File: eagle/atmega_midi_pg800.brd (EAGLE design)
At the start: 101 x 81 mm, 19 parts, among them IC1 78L05Z, U1 6N138, U2 ATMEGA328P_PDIP, X1 MAB6H

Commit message: routed
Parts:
- removed MIDI_IN1: MIDIJACK, adafruit:CP-2350
- removed RESET2: LSP11, solpad:LSP11
- added C4: 100uF, rcl:B45181A
- added C5: 10uF, rcl:B45181A
- added MIDI_THRU: MIDIJACK, adafruit:CP-2350
- added X2: 22-23-2081, con-molex:22-23-2081
- RESET: value LSP11 -> 22-23-2021; device solpad:LSP11 -> con-molex:22-23-2021
- moved D2 106.2 mm to (54.6, 17.8)
- moved IC1 102.8 mm to (45.7, 22.9), turned to 270 degrees
- moved X1 85.7 mm to (63.5, 7.62)
- moved R5 50.8 mm to (31.8, 19.1)
- moved RESET 6.14 mm to (24.1, 23.6), turned to 90 degrees
- moved R24 5.58 mm to (61.0, 21.6)
- moved D1 2.84 mm to (4.45, 26.0)
- moved R3 2.54 mm to (19.1, 30.5)
- moved C2 2.03 mm to (69.1, 24.1), turned to 90 degrees
- moved C3 1.98 mm to (30.5, 34.5), turned to 0 degrees
- moved R1 1.80 mm to (22.9, 31.8)
- moved U1 1.80 mm to (12.1, 27.3)
- moved Q1 1.80 mm to (61.0, 25.4)
- moved C1 0.25 mm to (53.1, 24.1), turned to 90 degrees
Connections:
- removed net PE: X1.PE, X1.PE@
- new net N$10: U2.16, X1.1
- new net N$11: U2.15, X1.5
- new net N$12: U2.23, X2.7
- new net N$13: U2.24, X2.6
- new net N$14: U2.25, X2.5
- new net N$15: U2.26, X2.4
- new net N$16: U2.27, X2.3
- new net N$17: U2.28, X2.2
- new net N$2: D2.A, X1.3
- new net N$6: C4.+, D2.C, IC1.3
- new net N$9: U2.14, X1.6
- net +5V: now also C5.+, IC1.1, X2.1
- net GND: now also C4.-, C5.-, IC1.2, MIDI_THRU.2, MIDI_THRU.PE, MIDI_THRU.PE1, MIDI_THRU.PE2, MIDI_THRU.PE@, RESET.1, X1.4, X1.PE, X1.PE@, X2.8; no longer MIDI_IN1.2, MIDI_IN1.PE, MIDI_IN1.PE1, MIDI_IN1.PE2, MIDI_IN1.PE@, RESET2.MP
- net N$1: now also MIDI_THRU.4; no longer MIDI_IN1.4
- net N$42: now also MIDI_THRU.5; no longer MIDI_IN1.5
- net N$43: now also RESET.2; no longer RESET.MP
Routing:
- net N$11: track 0.00 -> 49.1 mm
- net +5V: track 55.3 -> 86.3 mm
- net N$10: track 0.00 -> 27.2 mm
- net N$9: track 0.00 -> 20.1 mm
- net N$42: track 0.00 -> 19.9 mm
- net GND: track 226.8 -> 215.6 mm, vias 4 -> 0
- net N$6: track 0.00 -> 9.40 mm
- net N$7: track 23.9 -> 14.9 mm
- net N$2: track 0.00 -> 6.35 mm
- net N$3: track 21.7 -> 16.2 mm
- net N$43: track 11.4 -> 16.6 mm
- net N$17: track 0.00 -> 5.08 mm
- net N$16: track 0.00 -> 5.08 mm
- net N$15: track 0.00 -> 5.08 mm
- net N$14: track 0.00 -> 5.08 mm
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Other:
- board size 101 x 81 mm -> 100 x 80.8 mm

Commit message: gcode
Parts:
- Q1: value (none) -> 16.000Mhz
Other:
- outline, holes or cut-outs redrawn

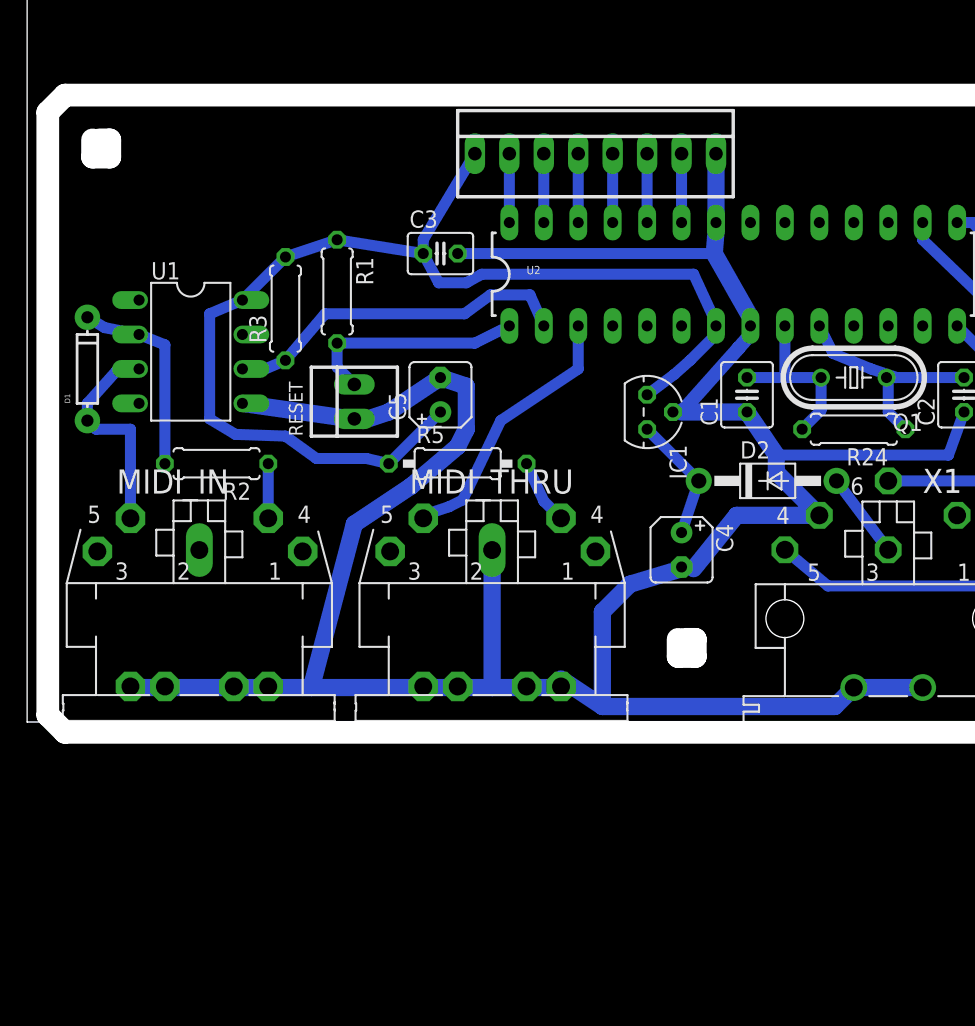
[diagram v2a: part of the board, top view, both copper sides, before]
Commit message: added oled disply connection
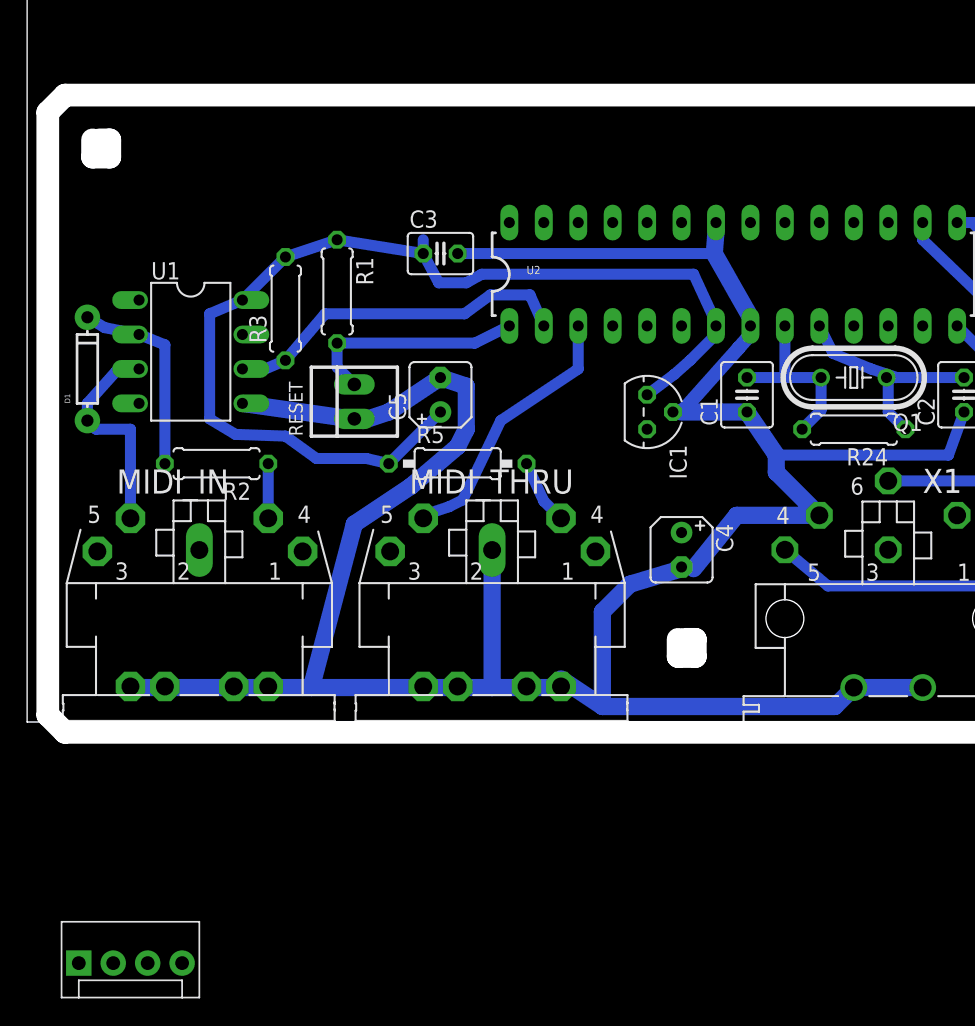
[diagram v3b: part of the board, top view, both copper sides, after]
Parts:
- removed D2: 1N4004, adafruit:DO41-10
- removed X2: 22-23-2081, con-molex:22-23-2081
- added DISPLAY: (no value), SparkFun-Connectors:MOLEX-1X4
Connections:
- removed net N$14: U2.25, X2.5
- removed net N$15: U2.26, X2.4
- removed net N$16: U2.27, X2.3
- removed net N$17: U2.28, X2.2
- removed net N$2: D2.A, X1.3
- net +5V: now also DISPLAY.1; no longer X2.1
- net GND: now also DISPLAY.2; no longer X2.8
- net N$12: now also DISPLAY.3, U2.28; no longer U2.23, X2.7
- net N$13: now also DISPLAY.4, U2.27; no longer U2.24, X2.6
- net N$6: now also X1.3; no longer D2.C
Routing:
- net N$6: track 9.40 -> 0.00 mm
- net +5V: track 86.3 -> 78.9 mm
- net N$2: track 6.35 -> 0.00 mm
- net N$17: track 5.08 -> 0.00 mm
- net N$16: track 5.08 -> 0.00 mm
- net N$15: track 5.08 -> 0.00 mm
- net N$14: track 5.08 -> 0.00 mm
- net N$13: track 5.08 -> 0.00 mm
- net N$12: track 5.08 -> 0.00 mm
- net GND: track 215.6 -> 210.5 mm
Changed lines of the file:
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@@
 <?xml version="1.0" encoding="utf-8"?>
 <!DOCTYPE eagle SYSTEM "eagle.dtd">
-<eagle version="7.6.0">
+<eagle version="7.7.0">
 <drawing>
 <settings>
@@
 </element>
 <element name="IC1" library="linear" package="TO92" value="78L05Z" x="45.72" y="22.86" rot="R270"/>
-<element name="D2" library="adafruit" package="DO41-10" value="1N4004" x="54.61" y="17.78"/>
 <element name="C4" library="rcl" package="B45181A" value="100uF" x="48.26" y="12.7" rot="R270"/>
 <element name="C5" library="rcl" package="B45181A" value="10uF" x="30.48" y="24.13" rot="R90"/>
@@
 <attribute name="MF" value="MOLEX" x="16.51" y="16.002" size="1.778" layer="27" rot="R90" display="off"/>
 </element>
-<element name="X2" library="con-molex" package="22-23-2081" value="22-23-2081" x="41.91" y="41.91">
-<attribute name="OC_NEWARK" value="01C7592" x="41.91" y="41.91" size="1.778" layer="27" display="off"/>
-<attribute name="MPN" value="22-23-2081" x="41.91" y="41.91" size="1.778" layer="27" display="off"/>
-<attribute name="OC_FARNELL" value="1756826" x="41.91" y="41.91" size="1.778" layer="27" display="off"/>
-<attribute name="MF" value="MOLEX" x="41.91" y="41.91" size="1.778" layer="27" display="off"/>
-</element>
+<element name="DISPLAY" library="SparkFun-Connectors" package="MOLEX-1X4" value="" x="3.81" y="-17.78"/>
 </elements>
 <signals>
@@
 <wire x1="30.353" y1="32.385" x2="32.385" y2="32.385" width="0.8128" layer="16"/>
 <wire x1="29.21" y1="34.544" x2="30.353" y2="32.385" width="0.8128" layer="16"/>
-<wire x1="33.02" y1="41.91" x2="29.21" y2="35.56" width="0.8128" layer="16"/>
 <wire x1="29.21" y1="35.56" x2="29.21" y2="34.544" width="0.8128" layer="16"/>
-<contactref element="X2" pad="1"/>
+<contactref element="DISPLAY" pad="1"/>
+<wire x1="3.81" y1="-17.78" x2="15.367" y2="21.209" width="0" layer="19" extent="16-16"/>
 </signal>
 <signal name="N$30">
@@
 <wire x1="55.245" y1="18.415" x2="58.42" y2="15.24" width="1.27" layer="16"/>
 <wire x1="17.78" y1="2.62" x2="15.24" y2="2.62" width="0.8128" layer="16"/>
-<contactref element="X2" pad="8"/>
-<wire x1="50.8" y1="41.91" x2="50.8" y2="36.83" width="1.27" layer="16"/>
+<contactref element="DISPLAY" pad="2"/>
+<wire x1="7.62" y1="2.54" x2="6.35" y2="-17.78" width="0" layer="19" extent="16-16"/>
 </signal>
 <signal name="N$42">
@@
 <wire x1="38.1" y1="16.29" x2="39.37" y2="15.02" width="0.8128" layer="16"/>
 </signal>
-<signal name="N$2">
-<contactref element="X1" pad="3"/>
-<contactref element="D2" pad="A"/>
-<wire x1="63.5" y1="12.7" x2="59.69" y2="17.78" width="0.8128" layer="16"/>
-</signal>
 <signal name="N$6">
-<contactref element="D2" pad="C"/>
 <contactref element="IC1" pad="3"/>
 <contactref element="C4" pad="+"/>
-<wire x1="49.53" y1="17.78" x2="45.72" y2="21.59" width="0.8128" layer="16"/>
-<wire x1="49.53" y1="17.78" x2="48.26" y2="13.97" width="0.8128" layer="16"/>
+<contactref element="X1" pad="3"/>
+<wire x1="48.26" y1="13.97" x2="63.5" y2="12.7" width="0" layer="19" extent="1-1"/>
+<wire x1="45.72" y1="21.59" x2="48.26" y2="13.97" width="0" layer="19" extent="1-1"/>
 </signal>
 <signal name="N$11">
@@
 </signal>
 <signal name="N$12">
-<contactref element="U2" pad="23"/>
-<contactref element="X2" pad="7"/>
-<wire x1="48.26" y1="36.83" x2="48.26" y2="41.91" width="0.8128" layer="16"/>
+<contactref element="DISPLAY" pad="3"/>
+<contactref element="U2" pad="28"/>
+<wire x1="8.89" y1="-17.78" x2="35.56" y2="36.83" width="0" layer="19" extent="1-1"/>
 </signal>
 <signal name="N$13">
-<contactref element="U2" pad="24"/>
-<contactref element="X2" pad="6"/>
-<wire x1="45.72" y1="41.91" x2="45.72" y2="36.83" width="0.8128" layer="16"/>
-</signal>
-<signal name="N$14">
-<contactref element="U2" pad="25"/>
-<contactref element="X2" pad="5"/>
-<wire x1="43.18" y1="36.83" x2="43.18" y2="41.91" width="0.8128" layer="16"/>
-</signal>
-<signal name="N$15">
-<contactref element="U2" pad="26"/>
-<contactref element="X2" pad="4"/>
-<wire x1="40.64" y1="41.91" x2="40.64" y2="36.83" width="0.8128" layer="16"/>
-</signal>
-<signal name="N$16">
+<contactref element="DISPLAY" pad="4"/>
 <contactref element="U2" pad="27"/>
-<contactref element="X2" pad="3"/>
-<wire x1="38.1" y1="36.83" x2="38.1" y2="41.91" width="0.8128" layer="16"/>
-</signal>
-<signal name="N$17">
-<contactref element="U2" pad="28"/>
-<contactref element="X2" pad="2"/>
-<wire x1="35.56" y1="41.91" x2="35.56" y2="36.83" width="0.8128" layer="16"/>
+<wire x1="11.43" y1="-17.78" x2="38.1" y2="36.83" width="0" layer="19" extent="1-1"/>
 </signal>
 </signals>

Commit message: mux coming in
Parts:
- added IC2, IC3, IC4: 4067N, 40xx:DIL24-6
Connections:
- new net N$14: IC3.1, U2.24
- new net N$15: IC2.1, U2.25
- new net N$2: IC4.1, U2.23
- new net VDD: IC2.24, IC3.24, IC4.24
- new net VSS: IC2.12, IC3.12, IC4.12
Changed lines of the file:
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@@
 </element>
 <element name="DISPLAY" library="SparkFun-Connectors" package="MOLEX-1X4" value="" x="3.81" y="-17.78"/>
+<element name="IC2" library="40xx" package="DIL24-6" value="4067N" x="15.24" y="-41.91"/>
+<element name="IC3" library="40xx" package="DIL24-6" value="4067N" x="15.24" y="-71.12"/>
+<element name="IC4" library="40xx" package="DIL24-6" value="4067N" x="15.24" y="-100.33"/>
 </elements>
 <signals>
@@
 <wire x1="11.43" y1="-17.78" x2="38.1" y2="36.83" width="0" layer="19" extent="1-1"/>
 </signal>
+<signal name="VSS">
+<contactref element="IC2" pad="12"/>
+<contactref element="IC3" pad="12"/>
+<contactref element="IC4" pad="12"/>
+<wire x1="29.21" y1="-78.74" x2="29.21" y2="-107.95" width="0" layer="19" extent="1-1"/>
+<wire x1="29.21" y1="-49.53" x2="29.21" y2="-78.74" width="0" layer="19" extent="1-1"/>
+</signal>
+<signal name="VDD">
+<contactref element="IC2" pad="24"/>
+<contactref element="IC3" pad="24"/>
+<contactref element="IC4" pad="24"/>
+<wire x1="1.27" y1="-63.5" x2="1.27" y2="-92.71" width="0" layer="19" extent="1-1"/>
+<wire x1="1.27" y1="-34.29" x2="1.27" y2="-63.5" width="0" layer="19" extent="1-1"/>
+</signal>
+<signal name="N$2">
+<contactref element="U2" pad="23"/>
+<contactref element="IC4" pad="1"/>
+<wire x1="48.26" y1="36.83" x2="1.27" y2="-107.95" width="0" layer="19" extent="1-1"/>
+</signal>
+<signal name="N$14">
+<contactref element="IC3" pad="1"/>
+<contactref element="U2" pad="24"/>
+<wire x1="1.27" y1="-78.74" x2="45.72" y2="36.83" width="0" layer="19" extent="1-1"/>
+</signal>
+<signal name="N$15">
+<contactref element="U2" pad="25"/>
+<contactref element="IC2" pad="1"/>
+<wire x1="1.27" y1="-49.53" x2="43.18" y2="36.83" width="0" layer="19" extent="1-1"/>
+</signal>
 </signals>

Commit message: muxes with input holes
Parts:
- added IN, IN1, IN10, IN11, IN12, IN2, IN3, IN4, IN5, IN6, IN7, IN8, IN9: 22-23-2041, con-molex:22-23-2041
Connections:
- new net N$16: IC2.10, IC3.10, IC4.10, U2.14
- new net N$17: IC2.11, IC3.11, IC4.11, U2.15
- new net N$18: IC2.14, IC3.14, IC4.14, U2.16
- new net N$19: IC2.13, IC3.13, IC4.13, U2.17
- net N$10: now also U2.11; no longer U2.16
- net N$11: now also U2.13; no longer U2.15
- net N$9: now also U2.12; no longer U2.14
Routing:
- net N$11: track 49.1 -> 0.00 mm
- net N$9: track 20.1 -> 16.5 mm
- net N$10: track 27.2 -> 26.0 mm
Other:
- outline, holes or cut-outs redrawn

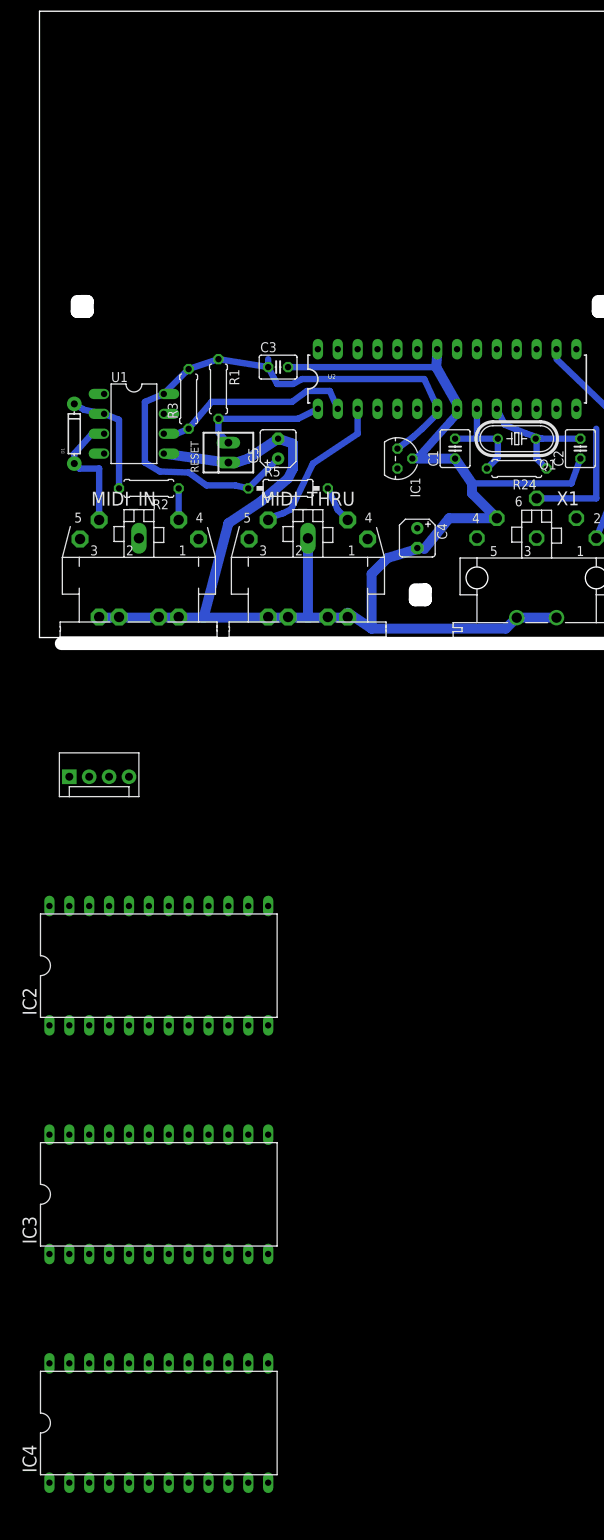
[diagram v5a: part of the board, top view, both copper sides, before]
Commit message: input terminals wired
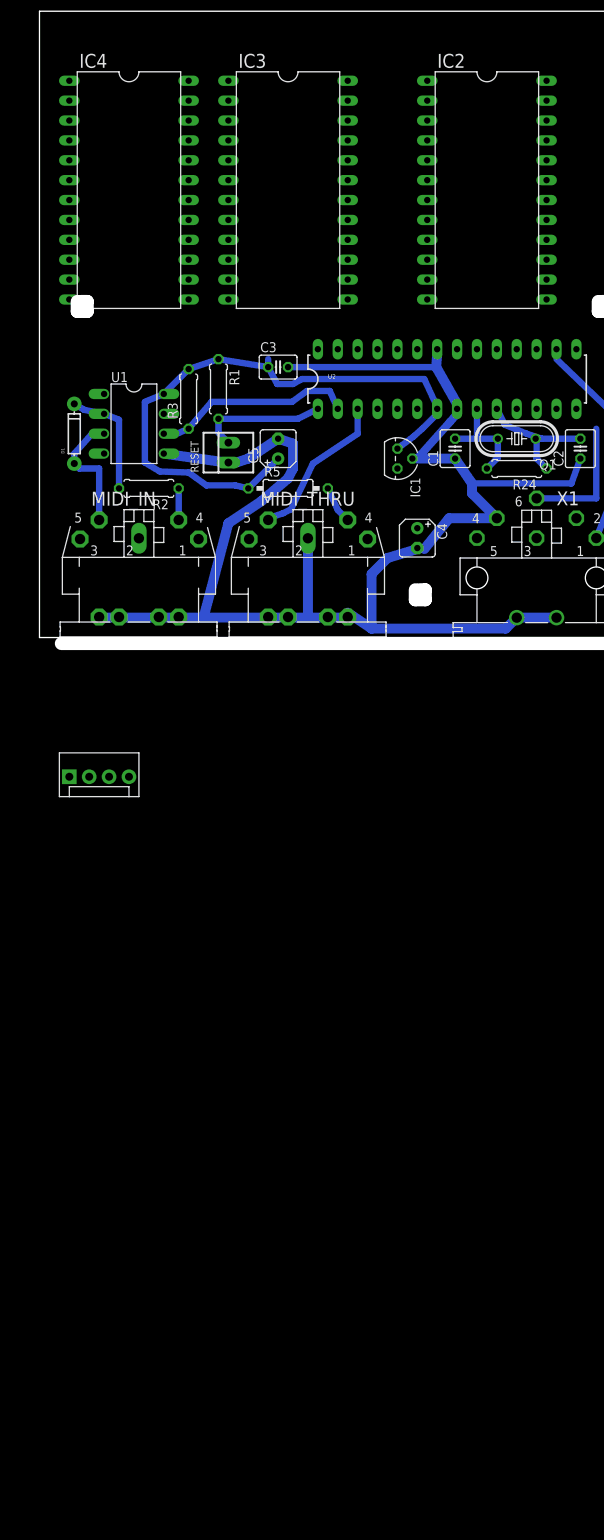
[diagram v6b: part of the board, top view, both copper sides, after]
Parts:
- moved IC4 157.5 mm to (11.4, 57.1), turned to 270 degrees
- moved IC3 129.3 mm to (31.8, 57.1), turned to 270 degrees
- moved IC2 107.6 mm to (57.1, 57.1), turned to 270 degrees
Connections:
- new net N$20: IC2.9, IN1.1
- new net N$21: IC2.8, IN1.2
- new net N$22: IC2.7, IN1.3
- new net N$23: IC2.6, IN1.4
- new net N$24: IC2.5, IN2.1
- new net N$25: IC2.4, IN2.2
- new net N$26: IC2.3, IN2.3
- new net N$27: IC2.2, IN2.4
- new net N$28: IC2.23, IN3.1
- new net N$29: IC2.22, IN3.2
- new net N$31: IC2.21, IN3.3
- new net N$32: IC2.20, IN3.4
- new net N$33: IC2.19, IN4.1
- new net N$34: IC2.18, IN4.2
- new net N$35: IC2.17, IN4.3
- new net N$36: IC2.16, IN4.4
- new net N$37: IC3.9, IN5.1
- new net N$38: IC3.8, IN5.2
- new net N$39: IC3.7, IN5.3
- new net N$40: IC3.6, IN5.4
- new net N$41: IC3.5, IN6.1
- new net N$44: IC3.4, IN6.2
- new net N$45: IC3.3, IN6.3
- new net N$46: IC3.2, IN6.4
- new net N$47: IC3.23, IN7.1
- new net N$48: IC3.22, IN7.2
- new net N$49: IC3.21, IN7.3
- new net N$50: IC3.20, IN7.4
- new net N$51: IC3.19, IN8.1
- new net N$52: IC3.18, IN8.2
- new net N$53: IC3.17, IN8.3
- new net N$54: IC3.16, IN8.4
- new net N$55: IC4.9, IN9.1
- new net N$56: IC4.8, IN9.2
- new net N$57: IC4.7, IN9.3
- new net N$58: IC4.6, IN9.4
- new net N$59: IC4.5, IN10.1
- new net N$60: IC4.4, IN10.2
- new net N$61: IC4.3, IN10.3
- new net N$62: IC4.2, IN10.4
- new net N$63: IC4.23, IN11.1
- new net N$64: IC4.22, IN11.2
- new net N$65: IC4.21, IN11.3
- new net N$66: IC4.20, IN11.4
- new net N$67: IC4.19, IN12.1
- new net N$68: IC4.18, IN12.2
- new net N$69: IC4.17, IN12.3
- new net N$70: IC4.16, IN12.4

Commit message: placement improved
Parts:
- removed IN: 22-23-2041, con-molex:22-23-2041
- added IN13, IN14, IN15, IN16: 22-23-2041, con-molex:22-23-2041
- moved IN12 366.6 mm to (30.5, 59.7), turned to 270 degrees
- moved IN11 361.5 mm to (30.5, 69.8), turned to 270 degrees
- moved IN10 345.4 mm to (3.81, 69.8), turned to 90 degrees
- moved IN9 320.1 mm to (3.81, 59.7), turned to 90 degrees
- moved IN8 310.1 mm to (63.5, 59.7), turned to 270 degrees
- moved IN7 305.1 mm to (63.5, 69.8), turned to 270 degrees
- moved IN6 286.2 mm to (38.1, 69.8), turned to 90 degrees
- moved IN5 261.0 mm to (38.1, 59.7), turned to 90 degrees
- moved IN4 260.0 mm to (96.5, 59.7), turned to 270 degrees
- moved IN3 255.2 mm to (96.5, 69.8), turned to 270 degrees
- moved IN2 232.7 mm to (71.1, 69.8), turned to 90 degrees
- moved IN1 208.4 mm to (71.1, 59.7), turned to 90 degrees
- moved DISPLAY 55.1 mm to (11.4, 36.8), turned to 180 degrees
- moved IC2 27.1 mm to (83.8, 62.2)
- moved IC3 19.7 mm to (50.8, 62.2)
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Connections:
- new net N$71: IC3.14, IN14.3
- new net N$72: IC3.13, IN14.4
- new net N$73: IC4.10, IN15.1
- new net N$74: IC4.11, IN15.2
- new net N$75: IC4.14, IN15.3
- new net N$76: IC4.13, IN15.4
- new net N$77: IN16.3, U2.16
- new net N$78: IN16.4, U2.17
- new net N$80: IC2.13, IN13.4
- new net N$81: IC2.14, IN13.3
- new net N$82: IC2.11, IN13.2
- new net N$83: IC2.10, IN13.1
- net GND: now also IC2.15, IC3.15, IC4.15
- net N$15: now also U2.23; no longer U2.25
- net N$16: now also IN16.1; no longer IC2.10, IC3.10, IC4.10
- net N$17: now also IN16.2; no longer IC2.11, IC3.11, IC4.11
- net N$18: now also IC3.10, IN14.1; no longer IC2.14, IC3.14, IC4.14, U2.16
- net N$19: now also IC3.11, IN14.2; no longer IC2.13, IC3.13, IC4.13, U2.17
- net N$2: now also U2.25; no longer U2.23
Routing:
- net N$10: track 26.0 -> 0.00 mm
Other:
- outline, holes or cut-outs redrawn
